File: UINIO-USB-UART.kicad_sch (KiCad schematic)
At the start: 34 parts, among them J1 Conn_01x07_Male, J2 Conn_01x04_Male, J3 Conn_01x03_Male, J4 Conn_01x06_Male, J5 Conn_01x06_Male, J6 Conn_01x04_Male, J7 Conn_01x06_Male, U1 CP2102, U2 CH343P

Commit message: Update schematic.
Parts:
- J4: renamed from J3; footprint (none) -> Connector_PinHeader_2.54mm:PinHeader_1x03_P2.54mm_Vertical
- renumbered J4 to J3
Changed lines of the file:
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@@
   (symbol (lib_id "Connector:Conn_01x06_Male") (at 184.15 146.05 180) (unit 1)
     (in_bom yes) (on_board yes)
-    (property "Reference" "J4" (id 0) (at 176.53 134.62 0))
+    (property "Reference" "J3" (id 0) (at 176.53 134.62 0))
     (property "Value" "Conn_01x06_Male" (id 1) (at 175.26 154.305 0))
     (property "Footprint" "Connector_PinHeader_2.54mm:PinHeader_1x06_P2.54mm_Vertical" (id 2) (at 184.15 146.05 0)
@@
   (symbol (lib_id "Connector:Conn_01x03_Male") (at 203.2 43.18 0) (unit 1)
     (in_bom yes) (on_board yes)
-    (property "Reference" "J3" (id 0) (at 214.63 36.83 0))
+    (property "Reference" "J4" (id 0) (at 214.63 36.83 0))
     (property "Value" "Conn_01x03_Male" (id 1) (at 213.36 48.26 0))
-    (property "Footprint" "" (id 2) (at 203.2 43.18 0)
+    (property "Footprint" "Connector_PinHeader_2.54mm:PinHeader_1x03_P2.54mm_Vertical" (id 2) (at 203.2 43.18 0)
       (effects (font (size 1.27 1.27)) hide)
     )
@@
       (reference "J2") (unit 1) (value "Conn_01x04_Male") (footprint "Connector_PinHeader_2.54mm:PinHeader_1x04_P2.54mm_Vertical")
     )
+    (path "/a843faee-19ed-4d4f-9388-6d6e796f9e13"
+      (reference "J3") (unit 1) (value "Conn_01x06_Male") (footprint "Connector_PinHeader_2.54mm:PinHeader_1x06_P2.54mm_Vertical")
+    )
     (path "/d88f613b-ca56-4260-baf9-c5e01fb8b7c4"
-      (reference "J3") (unit 1) (value "Conn_01x03_Male") (footprint "")
-    )
-    (path "/a843faee-19ed-4d4f-9388-6d6e796f9e13"
-      (reference "J4") (unit 1) (value "Conn_01x06_Male") (footprint "Connector_PinHeader_2.54mm:PinHeader_1x06_P2.54mm_Vertical")
+      (reference "J4") (unit 1) (value "Conn_01x03_Male") (footprint "Connector_PinHeader_2.54mm:PinHeader_1x03_P2.54mm_Vertical")
     )
     (path "/42d0fa17-b98e-4a54-8dd8-f9157e90541c"

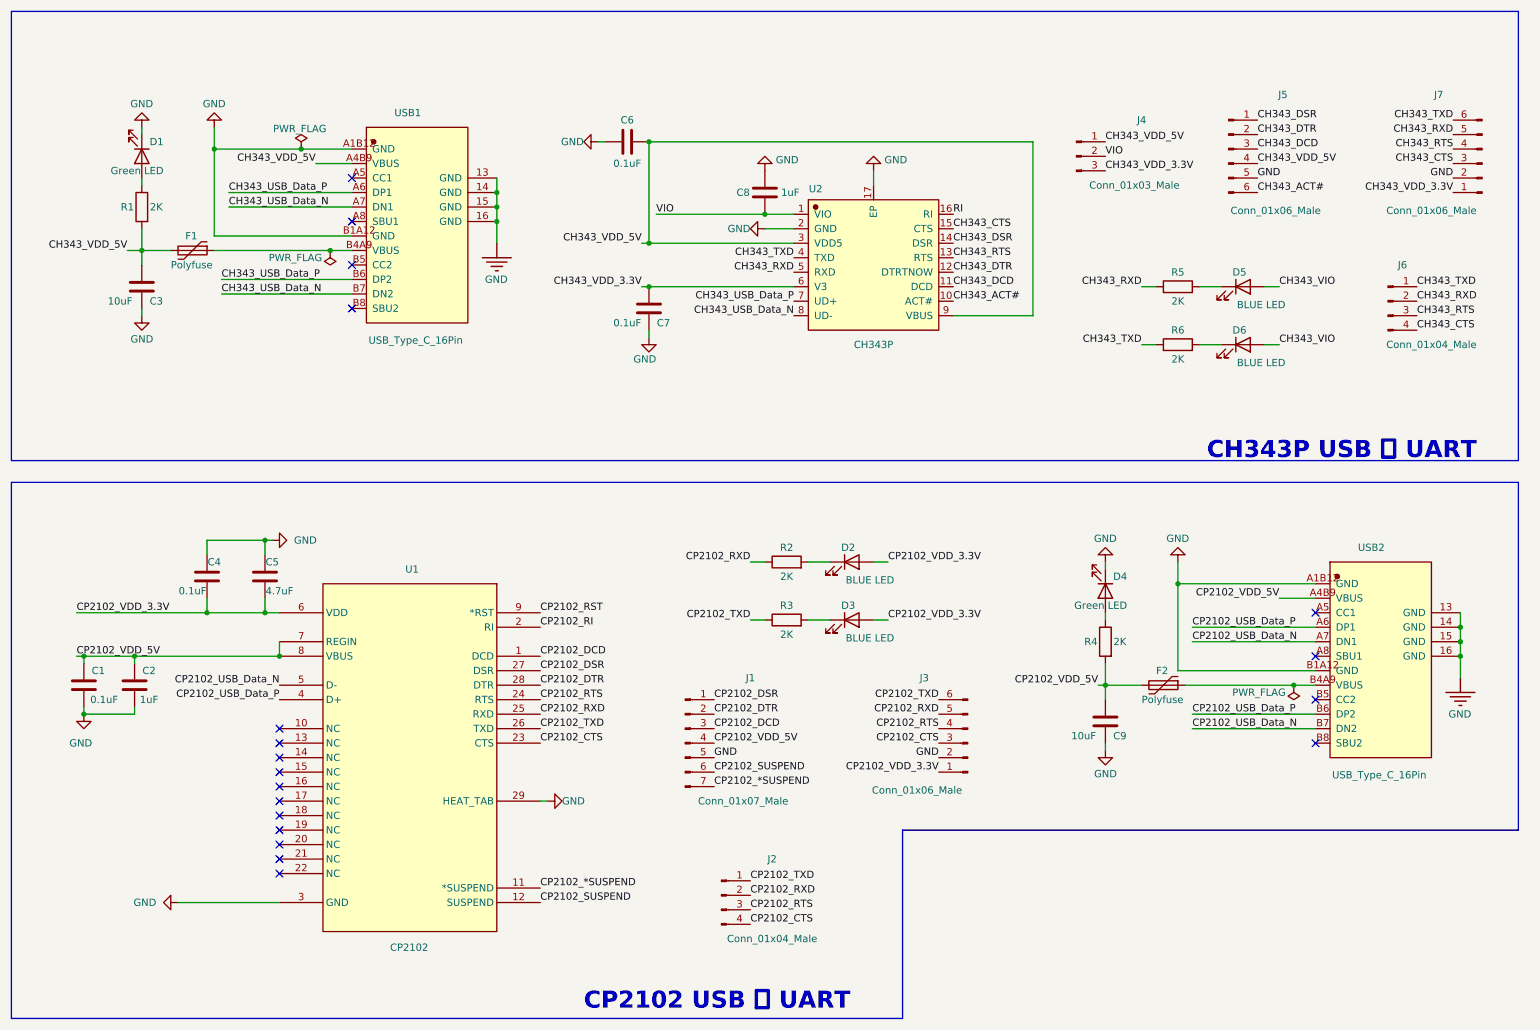
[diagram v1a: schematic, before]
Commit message: Complete component layout.
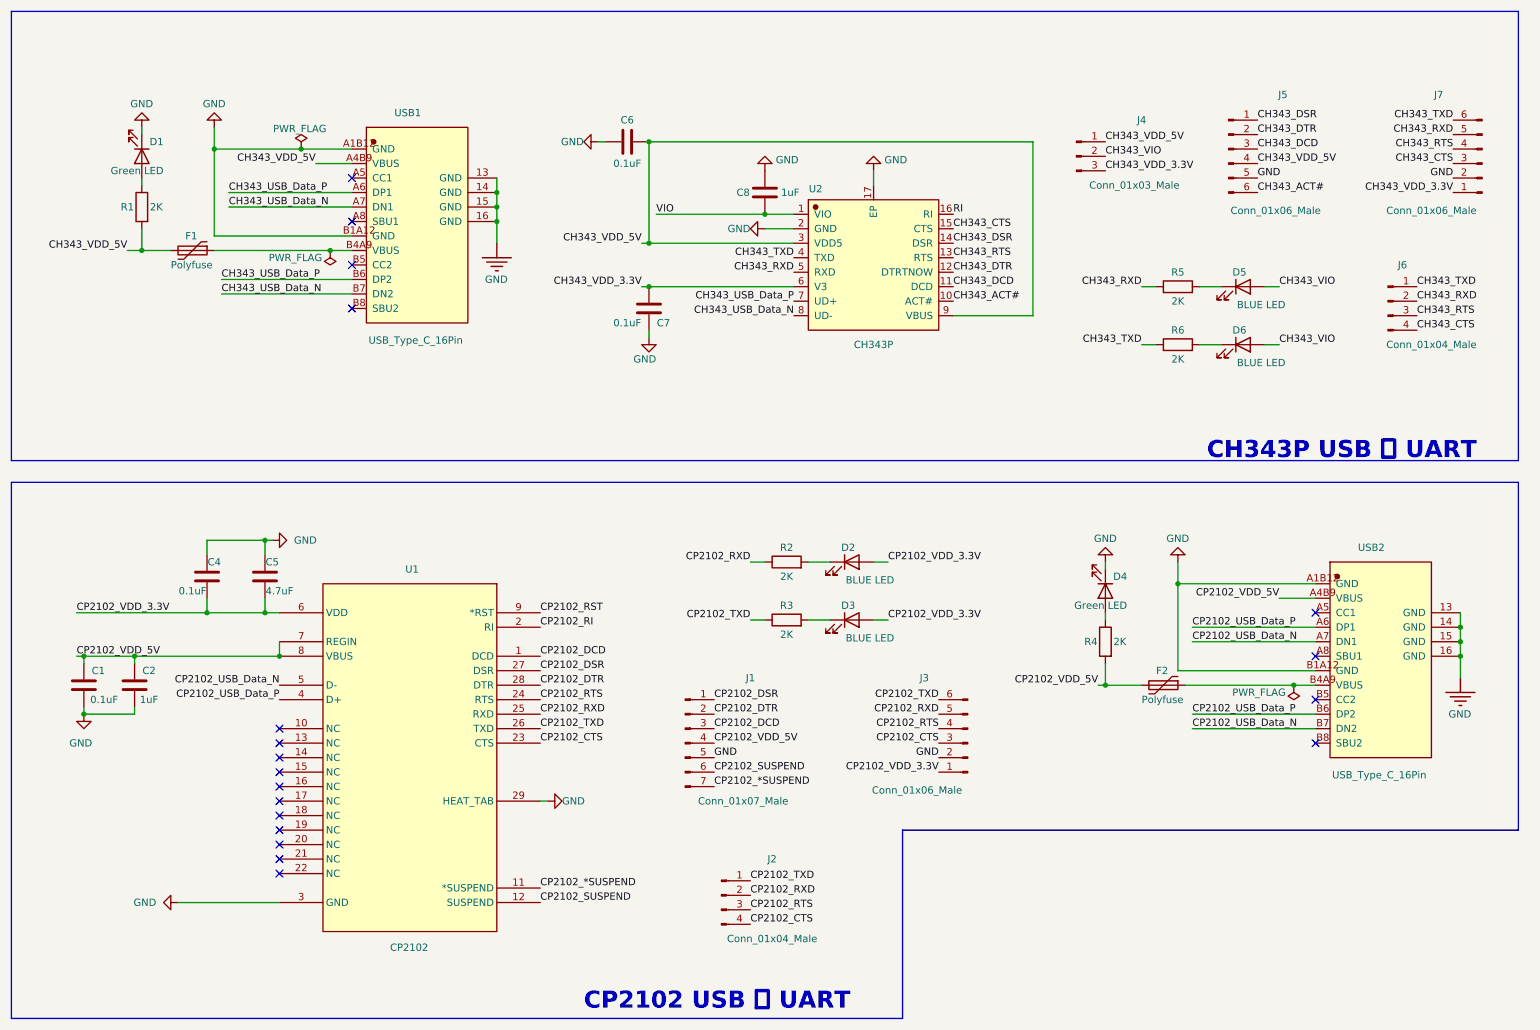
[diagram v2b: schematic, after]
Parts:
- removed C3, C9: 10uF, Capacitor_SMD:C_0603_1608Metric, symbol Device:C
- D1, D2, D3, D4, D5, D6: footprint LED_SMD:LED_0805_2012Metric -> LED_SMD:LED_0603_1608Metric
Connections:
- net CH343_VIO: now also J4.2 (Pin_2)
- net VIO: no longer J4.2 (Pin_2)
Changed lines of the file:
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@@
-    (stroke (width 0) (type default) (color 0 0 0 0))
-  )
-  (wire (pts (xy 39.37 69.85) (xy 39.37 71.12))
     (stroke (width 0) (type default) (color 0 0 0 0))
   )
@@
     (stroke (width 0) (type default) (color 0 0 0 0))
   )
-  (wire (pts (xy 208.28 138.43) (xy 208.28 135.89))
-    (stroke (width 0) (type default) (color 0 0 0 0))
-  )
   (wire (pts (xy 245.11 125.73) (xy 223.52 125.73))
     (stroke (width 0.254) (type default) (color 0 0 0 0))
@@
     (stroke (width 0) (type default) (color 0 0 0 0))
   )
-  (wire (pts (xy 39.37 59.69) (xy 39.37 62.23))
-    (stroke (width 0) (type default) (color 0 0 0 0))
-  )
   (wire (pts (xy 238.76 120.65) (xy 245.11 120.65))
     (stroke (width 0) (type default) (color 0 0 0 0))
@@
     (stroke (width 0) (type default) (color 0 0 0 0))
   )
-  (wire (pts (xy 208.28 146.05) (xy 208.28 147.32))
-    (stroke (width 0) (type default) (color 0 0 0 0))
-  )
   (polyline (pts (xy 16.51 96.52) (xy 280.67 96.52))
     (stroke (width 0) (type default) (color 0 0 0 0))
@@
     (effects (font (size 1.27 1.27)) (justify left bottom))
   )
-  (label "VIO" (at 208.28 43.18 0)
+  (label "CH343_VIO" (at 208.28 43.18 0)
     (effects (font (size 1.27 1.27)) (justify left bottom))
   )
@@
     (pin "1")
     (pin "2")
-  )
-  (symbol (lib_id "power:GND") (at 39.37 71.12 0) (mirror y) (unit 1)
-    (in_bom yes) (on_board yes)
-    (property "Reference" "#PWR03" (id 0) (at 39.37 77.47 0)
-      (effects (font (size 1.27 1.27)) hide)
-    )
-    (property "Value" "GND" (id 1) (at 37.3888 75.2348 0)
-      (effects (font (size 1.27 1.27)) (justify right))
-    )
-    (property "Footprint" "" (id 2) (at 39.37 71.12 0)
-      (effects (font (size 1.27 1.27)) hide)
-    )
-    (property "Datasheet" "" (id 3) (at 39.37 71.12 0)
-      (effects (font (size 1.27 1.27)) hide)
-    )
-    (pin "1")
   )
   (symbol (lib_id "power:GND") (at 148.59 45.72 180) (unit 1)
@@
     (property "Reference" "D2" (id 0) (at 163.195 111.76 0))
     (property "Value" "BLUE LED" (id 1) (at 167.005 117.475 0))
-    (property "Footprint" "LED_SMD:LED_0805_2012Metric" (id 2) (at 163.83 114.3 0)
+    (property "Footprint" "LED_SMD:LED_0603_1608Metric" (id 2) (at 163.83 114.3 0)
       (effects (font (size 1.27 1.27)) hide)
     )
@@
     )
     (pin "1")
-  )
-  (symbol (lib_id "Device:C") (at 208.28 142.24 0) (unit 1)
-    (in_bom yes) (on_board yes)
-    (property "Reference" "C9" (id 0) (at 210.82 144.78 0))
-    (property "Value" "10uF" (id 1) (at 204.47 144.78 0))
-    (property "Footprint" "Capacitor_SMD:C_0603_1608Metric" (id 2) (at 209.2452 146.05 0)
-      (effects (font (size 1.27 1.27)) hide)
-    )
-    (property "Datasheet" "~" (id 3) (at 208.28 142.24 0)
-      (effects (font (size 1.27 1.27)) hide)
-    )
-    (pin "1")
-    (pin "2")
   )
   (symbol (lib_id "Device:C") (at 148.59 49.53 180) (unit 1)
@@
       (effects (font (size 1.27 1.27)) (justify right))
     )
-    (property "Footprint" "LED_SMD:LED_0805_2012Metric" (id 2) (at 39.37 43.18 0)
+    (property "Footprint" "LED_SMD:LED_0603_1608Metric" (id 2) (at 39.37 43.18 0)
       (effects (font (size 1.27 1.27)) hide)
     )
@@
     (pin "1")
     (pin "2")
-  )
-  (symbol (lib_id "power:GND") (at 208.28 147.32 0) (mirror y) (unit 1)
-    (in_bom yes) (on_board yes)
-    (property "Reference" "#PWR015" (id 0) (at 208.28 153.67 0)
-      (effects (font (size 1.27 1.27)) hide)
-    )
-    (property "Value" "GND" (id 1) (at 206.2988 151.4348 0)
-      (effects (font (size 1.27 1.27)) (justify right))
-    )
-    (property "Footprint" "" (id 2) (at 208.28 147.32 0)
-      (effects (font (size 1.27 1.27)) hide)
-    )
-    (property "Datasheet" "" (id 3) (at 208.28 147.32 0)
-      (effects (font (size 1.27 1.27)) hide)
-    )
-    (pin "1")
   )
   (symbol (lib_id "Device:R") (at 220.98 66.04 90) (unit 1)
@@
       (effects (font (size 1.27 1.27)) (justify right))
     )
-    (property "Footprint" "LED_SMD:LED_0805_2012Metric" (id 2) (at 208.28 119.38 0)
+    (property "Footprint" "LED_SMD:LED_0603_1608Metric" (id 2) (at 208.28 119.38 0)
       (effects (font (size 1.27 1.27)) hide)
     )
@@
     (pin "2")
   )
-  (symbol (lib_id "Device:C") (at 39.37 66.04 0) (unit 1)
-    (in_bom yes) (on_board yes)
-    (property "Reference" "C3" (id 0) (at 41.91 68.58 0))
-    (property "Value" "10uF" (id 1) (at 35.56 68.58 0))
-    (property "Footprint" "Capacitor_SMD:C_0603_1608Metric" (id 2) (at 40.3352 69.85 0)
-      (effects (font (size 1.27 1.27)) hide)
-    )
-    (property "Datasheet" "~" (id 3) (at 39.37 66.04 0)
-      (effects (font (size 1.27 1.27)) hide)
-    )
-    (pin "1")
-    (pin "2")
-  )
   (symbol (lib_id "Device:LED") (at 232.41 76.2 0) (unit 1)
     (in_bom yes) (on_board yes)
     (property "Reference" "D6" (id 0) (at 231.775 73.66 0))
     (property "Value" "BLUE LED" (id 1) (at 235.585 79.375 0))
-    (property "Footprint" "LED_SMD:LED_0805_2012Metric" (id 2) (at 232.41 76.2 0)
+    (property "Footprint" "LED_SMD:LED_0603_1608Metric" (id 2) (at 232.41 76.2 0)
       (effects (font (size 1.27 1.27)) hide)
     )
@@
     (property "Reference" "D5" (id 0) (at 231.775 63.5 0))
     (property "Value" "BLUE LED" (id 1) (at 235.585 69.215 0))
-    (property "Footprint" "LED_SMD:LED_0805_2012Metric" (id 2) (at 232.41 66.04 0)
+    (property "Footprint" "LED_SMD:LED_0603_1608Metric" (id 2) (at 232.41 66.04 0)
       (effects (font (size 1.27 1.27)) hide)
     )
@@
     (property "Reference" "D3" (id 0) (at 163.195 121.92 0))
     (property "Value" "BLUE LED" (id 1) (at 167.005 127.635 0))
-    (property "Footprint" "LED_SMD:LED_0805_2012Metric" (id 2) (at 163.83 124.46 0)
+    (property "Footprint" "LED_SMD:LED_0603_1608Metric" (id 2) (at 163.83 124.46 0)
       (effects (font (size 1.27 1.27)) hide)
     )
@@
       (reference "#PWR02") (unit 1) (value "GND") (footprint "")
     )
-    (path "/2ed74ffb-0a72-46ed-8353-a4f8c50f02f6"
-      (reference "#PWR03") (unit 1) (value "GND") (footprint "")
-    )
     (path "/d29ebf22-b72c-40ef-b309-aa197600a1b0"
       (reference "#PWR04") (unit 1) (value "GND") (footprint "")
@@
       (reference "#PWR014") (unit 1) (value "GND") (footprint "")
     )
-    (path "/595cf4f0-44b7-4a37-b6de-d705b6d78169"
-      (reference "#PWR015") (unit 1) (value "GND") (footprint "")
-    )
     (path "/145986b0-c659-4af1-a8d4-17297279c7c5"
       (reference "#PWR016") (unit 1) (value "GND") (footprint "")
@@
       (reference "C2") (unit 1) (value "1uF") (footprint "Capacitor_SMD:C_0603_1608Metric")
     )
-    (path "/877bdb4c-dd70-4d29-92b3-dbe5e579cfab"
-      (reference "C3") (unit 1) (value "10uF") (footprint "Capacitor_SMD:C_0603_1608Metric")
-    )
     (path "/6905462b-ad9e-4bd0-8f8f-b20e58d07425"
       (reference "C4") (unit 1) (value "0.1uF") (footprint "Capacitor_SMD:C_0603_1608Metric")
@@
       (reference "C8") (unit 1) (value "1uF") (footprint "Capacitor_SMD:C_0603_1608Metric")
     )
-    (path "/4822adff-936d-43ad-9487-806699050c6b"
-      (reference "C9") (unit 1) (value "10uF") (footprint "Capacitor_SMD:C_0603_1608Metric")
-    )
     (path "/58880072-0bf5-4033-85aa-cea4a3a20cc6"
-      (reference "D1") (unit 1) (value "Green LED") (footprint "LED_SMD:LED_0805_2012Metric")
+      (reference "D1") (unit 1) (value "Green LED") (footprint "LED_SMD:LED_0603_1608Metric")
     )
     (path "/4355f3d7-416a-4a2a-be55-e7f457668f2e"
-      (reference "D2") (unit 1) (value "BLUE LED") (footprint "LED_SMD:LED_0805_2012Metric")
+      (reference "D2") (unit 1) (value "BLUE LED") (footprint "LED_SMD:LED_0603_1608Metric")
     )
     (path "/9a6ca70b-5ce8-4d3a-a9b0-52996f4467cc"
-      (reference "D3") (unit 1) (value "BLUE LED") (footprint "LED_SMD:LED_0805_2012Metric")
+      (reference "D3") (unit 1) (value "BLUE LED") (footprint "LED_SMD:LED_0603_1608Metric")
     )
     (path "/60946db8-e87e-460e-a9d9-488015328ebc"
-      (reference "D4") (unit 1) (value "Green LED") (footprint "LED_SMD:LED_0805_2012Metric")
+      (reference "D4") (unit 1) (value "Green LED") (footprint "LED_SMD:LED_0603_1608Metric")
     )
     (path "/93c9daf9-d01f-4d37-84f1-5d768955502f"
-      (reference "D5") (unit 1) (value "BLUE LED") (footprint "LED_SMD:LED_0805_2012Metric")
+      (reference "D5") (unit 1) (value "BLUE LED") (footprint "LED_SMD:LED_0603_1608Metric")
     )
     (path "/8882ae6e-0dba-4236-a656-f22c9574fe10"
-      (reference "D6") (unit 1) (value "BLUE LED") (footprint "LED_SMD:LED_0805_2012Metric")
+      (reference "D6") (unit 1) (value "BLUE LED") (footprint "LED_SMD:LED_0603_1608Metric")
     )
     (path "/8126ee68-d3d5-4ad8-950d-d19283d76e5a"

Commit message: PCB layout finish.
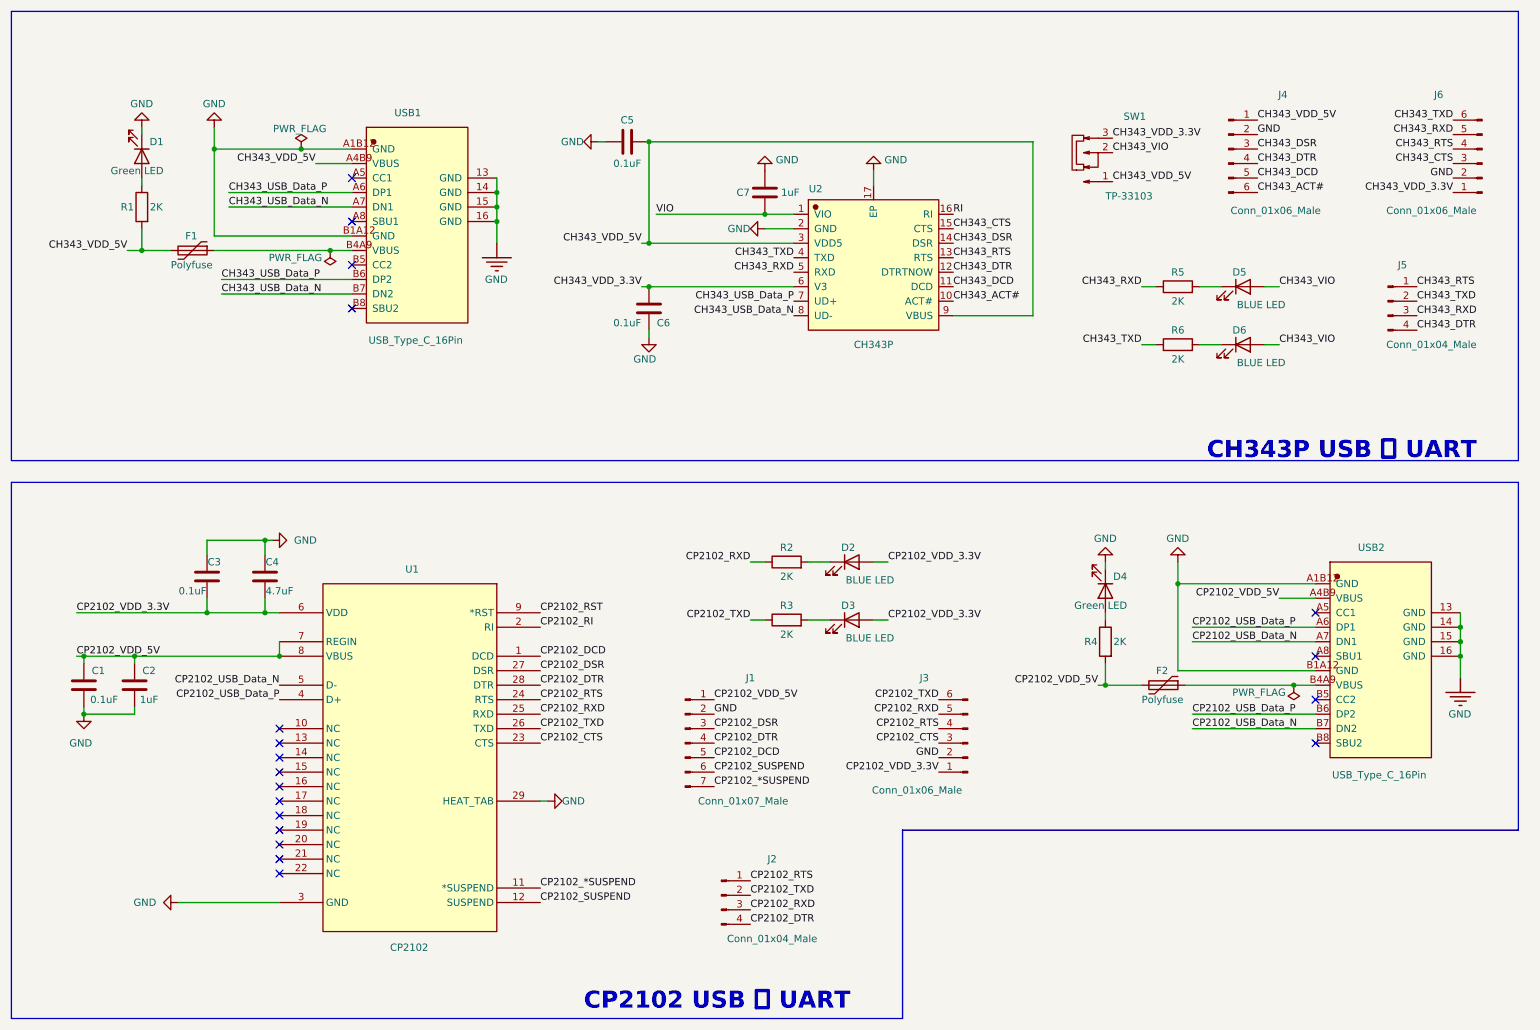
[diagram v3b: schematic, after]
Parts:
- removed J4: Conn_01x03_Male, Connector_PinHeader_2.54mm:PinHeader_1x03_P2.54mm_Vertical, symbol Connector:Conn_01x03_Male
- added SW1: TP-33103, Uinio:SW-TH_ROCPU_TP-33103, symbol Uinio:TP-33103
- renumbered C4 to C3, C5 to C4, C6 to C5, C7 to C6, C8 to C7, J5 to J4, J6 to J5, J7 to J6
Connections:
- net CH343_CTS: no longer J5.4 (Pin_4)
- net CH343_DCD: now also J4.5 (Pin_5); no longer J4.3 (Pin_3)
- net CH343_DSR: now also J4.3 (Pin_3); no longer J4.1 (Pin_1)
- net CH343_DTR: now also J4.4 (Pin_4), J5.4 (Pin_4); no longer J4.2 (Pin_2)
- net CH343_RTS: now also J5.1 (Pin_1); no longer J5.3 (Pin_3)
- net CH343_RXD: now also J5.3 (Pin_3); no longer J5.2 (Pin_2)
- net CH343_TXD: now also J5.2 (Pin_2); no longer J5.1 (Pin_1)
- net CH343_VDD_3.3V: now also SW1.3
- net CH343_VDD_5V: now also J4.1 (Pin_1), SW1.1; no longer J4.4 (Pin_4)
- net CH343_VIO: now also SW1.2
- net CP2102_CTS: no longer J2.4 (Pin_4)
- net CP2102_DCD: now also J1.5 (Pin_5); no longer J1.3 (Pin_3)
- net CP2102_DSR: now also J1.3 (Pin_3); no longer J1.1 (Pin_1)
- net CP2102_DTR: now also J1.4 (Pin_4), J2.4 (Pin_4); no longer J1.2 (Pin_2)
- net CP2102_RTS: now also J2.1 (Pin_1); no longer J2.3 (Pin_3)
- net CP2102_RXD: now also J2.3 (Pin_3); no longer J2.2 (Pin_2)
- net CP2102_TXD: now also J2.2 (Pin_2); no longer J2.1 (Pin_1)
- net CP2102_VDD_5V: now also J1.1 (Pin_1); no longer J1.4 (Pin_4)
- net GND: now also J1.2 (Pin_2), J4.2 (Pin_2); no longer J1.5 (Pin_5), J4.5 (Pin_5)

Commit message: Finish layout.
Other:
- company: (none) -> 电子技术博客 UinIO.com
- title: (none) -> UINIO-USB-UART
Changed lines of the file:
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@@
 (kicad_sch (version 20211123) (generator eeschema)
   (paper "A4")
+  (title_block
+    (title "UINIO-USB-UART")
+    (date "2022-10-11")
+    (rev "Hank")
+    (company "电子技术博客 UinIO.com")
+  )
   (junction (at 148.59 53.34) (diameter 0) (color 0 0 0 0)
   )
